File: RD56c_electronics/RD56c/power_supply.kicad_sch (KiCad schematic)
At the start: 31 parts, among them U201 TPS54202DDC, U202 TPS54202DDC

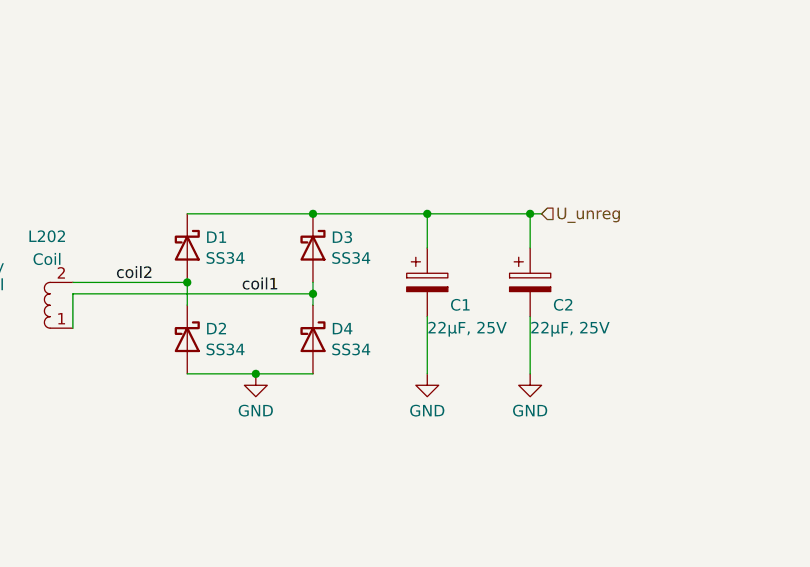
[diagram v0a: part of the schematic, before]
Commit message: added empty_sheet.kicad_wks to KiCAD folders
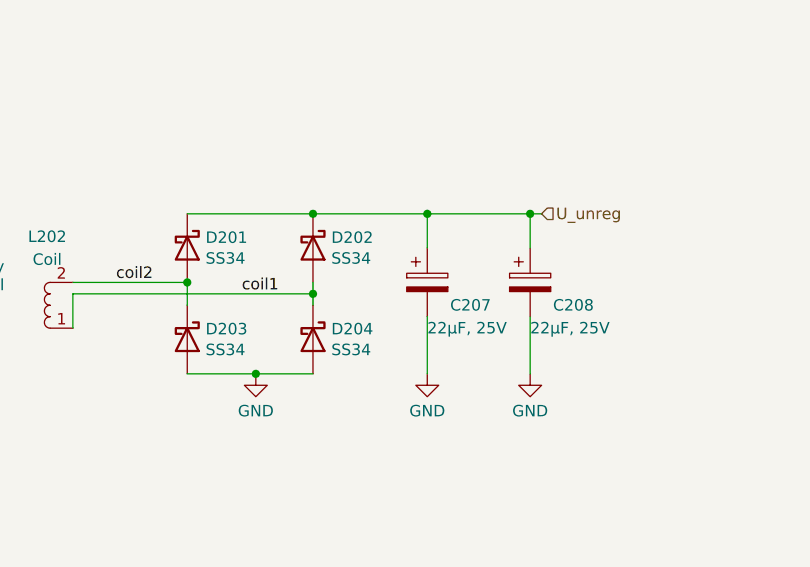
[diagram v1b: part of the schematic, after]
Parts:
- renumbered C1 to C207, C2 to C208, D1 to D201, D3 to D202, D2 to D203, D4 to D204
